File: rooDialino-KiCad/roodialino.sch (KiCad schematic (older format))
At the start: 50 parts, among them J1 Raspi Connector, J2 ICSP, J3 FTDI, J4 2nd IRX, J5 IR LED, Q1 2N7002, Q2 2N7002, Q3 2N7002, SW1 SW_Push, U1 ATmega328P, U2 TSOP34838, U3 TXS0108EPW, Y1 16 MHz

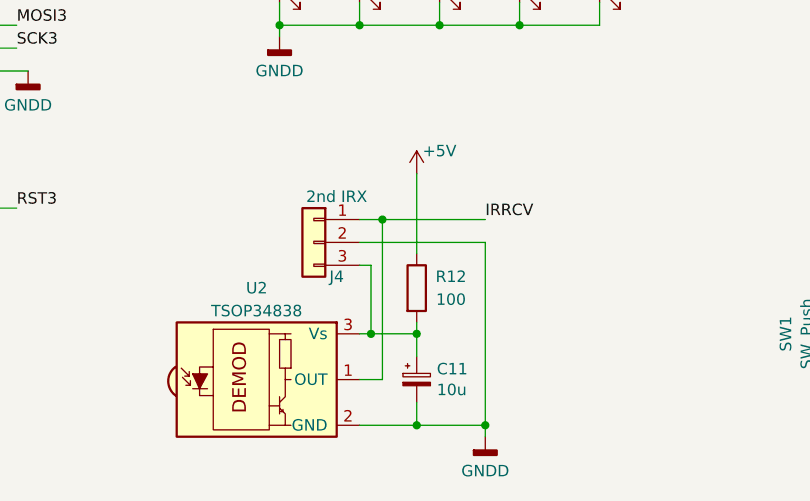
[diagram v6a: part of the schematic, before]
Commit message: Reroute to 0402 complete. Also, bugs fixed
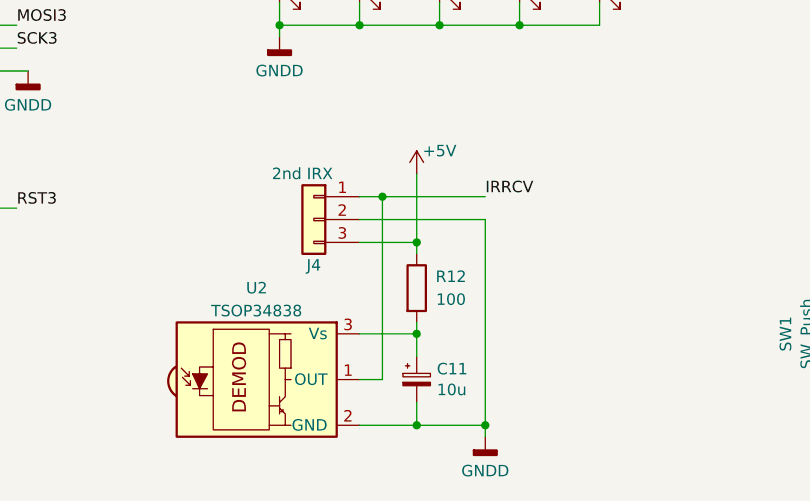
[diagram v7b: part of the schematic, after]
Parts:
- C10, C12, C3, C6, C9: footprint Capacitor_SMD:C_0603_1608Metric -> Capacitor_SMD:C_0402_1005Metric; LCSC C14663 -> C1525
- D4: footprint LED_SMD:LED_0805_2012Metric -> LED_SMD:LED_0603_1608Metric; LCSC C84256 -> C72038
- D5: footprint LED_SMD:LED_0805_2012Metric -> LED_SMD:LED_0603_1608Metric; LCSC C2297 -> C72043
- D6, D7, D8: LCSC (none) -> C55528
- R11: footprint Resistor_SMD:R_0805_2012Metric -> Resistor_SMD:R_0603_1608Metric; LCSC C17634 -> C25105
- R12: footprint Resistor_SMD:R_0603_1608Metric -> Resistor_SMD:R_0402_1005Metric; LCSC C2275 -> C25076
- R2, R3, R4, R5, R6: footprint Resistor_SMD:R_0805_2012Metric -> Resistor_SMD:R_0402_1005Metric; LCSC C17710 -> C25117
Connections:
- net +5V: now also J4.3 (Pin_3)
- net at C11.1, R12.2, U2.3 (Vs): no longer J4.3 (Pin_3)
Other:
- moved on the sheet: J4
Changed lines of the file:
@@
 F 0 "C6" V 3200 1500 50  0000 R CNN
 F 1 "100n" V 3300 1550 50  0000 R CNN
-F 2 "Capacitor_SMD:C_0603_1608Metric" H 3150 1350 50  0001 C CNN
+F 2 "Capacitor_SMD:C_0402_1005Metric" H 3150 1350 50  0001 C CNN
 F 3 "~" H 3150 1350 50  0001 C CNN
-F 4 "C14663" V 3150 1350 50  0001 C CNN "LCSC"
+F 4 "C1525" V 3150 1350 50  0001 C CNN "LCSC"
 	1    3150 1350
 	0    1    1    0
@@
 F 0 "D4" V 4150 5200 50  0000 R CNN
 F 1 "LED" V 4050 5200 50  0000 R CNN
-F 2 "LED_SMD:LED_0805_2012Metric" H 4100 5300 50  0001 C CNN
-F 3 "~" H 4100 5300 50  0001 C CNN
-F 4 "C84256" V 4100 5300 50  0001 C CNN "LCSC"
+F 2 "LED_SMD:LED_0603_1608Metric" H 4100 5300 50  0001 C CNN
+F 3 "https://datasheet.lcsc.com/lcsc/1810101813_Everlight-Elec-19-213-Y2C-CQ2R2L-3T-CY_C72038.pdf" H 4100 5300 50  0001 C CNN
+F 4 "C72038" V 4100 5300 50  0001 C CNN "LCSC"
 	1    4100 5300
 	0    -1   -1   0
@@
 F 0 "D5" V 4500 5200 50  0000 R CNN
 F 1 "LED" V 4400 5200 50  0000 R CNN
-F 2 "LED_SMD:LED_0805_2012Metric" H 4450 5300 50  0001 C CNN
-F 3 "~" H 4450 5300 50  0001 C CNN
-F 4 "C2297" V 4450 5300 50  0001 C CNN "LCSC"
+F 2 "LED_SMD:LED_0603_1608Metric" H 4450 5300 50  0001 C CNN
+F 3 "https://datasheet.lcsc.com/lcsc/1811101510_Everlight-Elec-19-217-GHC-YR1S2-3T_C72043.pdf" H 4450 5300 50  0001 C CNN
+F 4 "C72043" V 4450 5300 50  0001 C CNN "LCSC"
 	1    4450 5300
 	0    -1   -1   0
@@
 F 0 "R2" H 2900 4850 50  0000 C CNN
 F 1 "470" H 2900 4950 50  0000 C CNN
-F 2 "Resistor_SMD:R_0805_2012Metric" V 2980 4900 50  0001 C CNN
+F 2 "Resistor_SMD:R_0402_1005Metric" V 2980 4900 50  0001 C CNN
 F 3 "~" H 3050 4900 50  0001 C CNN
-F 4 "C17710" H 3050 4900 50  0001 C CNN "LCSC"
+F 4 "C25117" H 3050 4900 50  0001 C CNN "LCSC"
 	1    3050 4900
 	-1   0    0    1
@@
 F 0 "R3" H 3250 4850 50  0000 C CNN
 F 1 "470" H 3250 4950 50  0000 C CNN
-F 2 "Resistor_SMD:R_0805_2012Metric" V 3330 4900 50  0001 C CNN
+F 2 "Resistor_SMD:R_0402_1005Metric" V 3330 4900 50  0001 C CNN
 F 3 "~" H 3400 4900 50  0001 C CNN
-F 4 "C17710" H 3400 4900 50  0001 C CNN "LCSC"
+F 4 "C25117" H 3400 4900 50  0001 C CNN "LCSC"
 	1    3400 4900
 	-1   0    0    1
@@
 F 0 "R4" H 3600 4850 50  0000 C CNN
 F 1 "470" H 3600 4950 50  0000 C CNN
-F 2 "Resistor_SMD:R_0805_2012Metric" V 3680 4900 50  0001 C CNN
+F 2 "Resistor_SMD:R_0402_1005Metric" V 3680 4900 50  0001 C CNN
 F 3 "~" H 3750 4900 50  0001 C CNN
-F 4 "C17710" H 3750 4900 50  0001 C CNN "LCSC"
+F 4 "C25117" H 3750 4900 50  0001 C CNN "LCSC"
 	1    3750 4900
 	-1   0    0    1
@@
 F 0 "R5" H 3950 4850 50  0000 C CNN
 F 1 "470" H 3950 4950 50  0000 C CNN
-F 2 "Resistor_SMD:R_0805_2012Metric" V 4030 4900 50  0001 C CNN
+F 2 "Resistor_SMD:R_0402_1005Metric" V 4030 4900 50  0001 C CNN
 F 3 "~" H 4100 4900 50  0001 C CNN
-F 4 "C17710" H 4100 4900 50  0001 C CNN "LCSC"
+F 4 "C25117" H 4100 4900 50  0001 C CNN "LCSC"
 	1    4100 4900
 	-1   0    0    1
@@
 F 0 "R6" H 4300 4850 50  0000 C CNN
 F 1 "470" H 4300 4950 50  0000 C CNN
-F 2 "Resistor_SMD:R_0805_2012Metric" V 4380 4900 50  0001 C CNN
+F 2 "Resistor_SMD:R_0402_1005Metric" V 4380 4900 50  0001 C CNN
 F 3 "~" H 4450 4900 50  0001 C CNN
-F 4 "C17710" H 4450 4900 50  0001 C CNN "LCSC"
+F 4 "C25117" H 4450 4900 50  0001 C CNN "LCSC"
 	1    4450 4900
 	-1   0    0    1
@@
 F 1 "LED" H 4900 1900 50  0000 R CNN
 F 2 "LED_THT:LED_D5.0mm_IRBlack" H 4850 1700 50  0001 C CNN
-F 3 "~" H 4850 1700 50  0001 C CNN
+F 3 "https://datasheet.lcsc.com/lcsc/1809200025_Vishay-Intertech-TSAL6200_C55528.pdf" H 4850 1700 50  0001 C CNN
+F 4 "C55528" H 4850 1700 50  0001 C CNN "LCSC"
 	1    4850 1700
 	-1   0    0    1
@@
 F 1 "LED" H 5250 1900 50  0000 R CNN
 F 2 "LED_THT:LED_D5.0mm_Horizontal_O1.27mm_Z3.0mm_IRBlack" H 5200 1700 50  0001 C CNN
-F 3 "~" H 5200 1700 50  0001 C CNN
+F 3 "https://datasheet.lcsc.com/lcsc/1809200025_Vishay-Intertech-TSAL6200_C55528.pdf" H 5200 1700 50  0001 C CNN
+F 4 "C55528" H 5200 1700 50  0001 C CNN "LCSC"
 	1    5200 1700
 	-1   0    0    1
@@
 F 1 "LED" H 4550 1900 50  0000 R CNN
 F 2 "LED_THT:LED_D5.0mm_Horizontal_O1.27mm_Z3.0mm_IRBlack" H 4500 1700 50  0001 C CNN
-F 3 "~" H 4500 1700 50  0001 C CNN
+F 3 "https://datasheet.lcsc.com/lcsc/1809200025_Vishay-Intertech-TSAL6200_C55528.pdf" H 4500 1700 50  0001 C CNN
+F 4 "C55528" H 4500 1700 50  0001 C CNN "LCSC"
 	1    4500 1700
 	-1   0    0    1
@@
 F 0 "R11" H 5500 1350 50  0000 C CNN
 F 1 "33" H 5500 1250 50  0000 C CNN
-F 2 "Resistor_SMD:R_0805_2012Metric" V 5330 1300 50  0001 C CNN
+F 2 "Resistor_SMD:R_0603_1608Metric" V 5330 1300 50  0001 C CNN
 F 3 "~" H 5400 1300 50  0001 C CNN
-F 4 "C17634" H 5400 1300 50  0001 C CNN "LCSC"
+F 4 "C25105" H 5400 1300 50  0001 C CNN "LCSC"
 	1    5400 1300
 	1    0    0    -1
@@
 	1    0    0    -1
 $EndComp
-Text Label 3950 6400 0    50   ~ 0
+Text Label 3950 6300 0    50   ~ 0
 IRRCV
-$Comp
-L Connector_Generic:Conn_01x03 J4
-U 1 1 61933FD4
-P 3200 6500
-F 0 "J4" H 3100 6350 50  0000 C CNN
-F 1 "2nd IRX" H 3100 6700 50  0000 C CNN
-F 2 "Connector_PinHeader_2.54mm:PinHeader_1x03_P2.54mm_Vertical" H 3200 6500 50  0001 C CNN
-F 3 "~" H 3200 6500 50  0001 C CNN
-	1    3200 6500
-	-1   0    0    -1
-$EndComp
 $Comp
 L Connector_Generic:Conn_02x20_Odd_Even J1
@@
 F 0 "C3" H 2400 5150 50  0000 R CNN
 F 1 "100n" H 2600 4850 50  0000 R CNN
-F 2 "Capacitor_SMD:C_0603_1608Metric" H 2350 4950 50  0001 C CNN
+F 2 "Capacitor_SMD:C_0402_1005Metric" H 2350 4950 50  0001 C CNN
 F 3 "~" H 2350 4950 50  0001 C CNN
-F 4 "C14663" H 2350 4950 50  0001 C CNN "LCSC"
+F 4 "C1525" H 2350 4950 50  0001 C CNN "LCSC"
 	1    2350 4950
 	1    0    0    -1
@@
 F 0 "C9" H 5250 1100 50  0000 R CNN
 F 1 "100n" H 5300 950 50  0000 R CNN
-F 2 "Capacitor_SMD:C_0603_1608Metric" H 5050 1050 50  0001 C CNN
+F 2 "Capacitor_SMD:C_0402_1005Metric" H 5050 1050 50  0001 C CNN
 F 3 "~" H 5050 1050 50  0001 C CNN
-F 4 "C14663" H 5050 1050 50  0001 C CNN "LCSC"
+F 4 "C1525" H 5050 1050 50  0001 C CNN "LCSC"
 	1    5050 1050
 	1    0    0    -1
@@
 F 0 "C12" H 6500 4300 50  0000 R CNN
 F 1 "100n" H 6550 4200 50  0000 R CNN
-F 2 "Capacitor_SMD:C_0603_1608Metric" H 6300 4250 50  0001 C CNN
+F 2 "Capacitor_SMD:C_0402_1005Metric" H 6300 4250 50  0001 C CNN
 F 3 "~" H 6300 4250 50  0001 C CNN
-F 4 "C14663" H 6300 4250 50  0001 C CNN "LCSC"
+F 4 "C1525" H 6300 4250 50  0001 C CNN "LCSC"
 	1    6300 4250
 	1    0    0    -1
@@
 F 0 "C10" H 5800 4300 50  0000 R CNN
 F 1 "100n" H 5850 4200 50  0000 R CNN
-F 2 "Capacitor_SMD:C_0603_1608Metric" H 5900 4250 50  0001 C CNN
+F 2 "Capacitor_SMD:C_0402_1005Metric" H 5900 4250 50  0001 C CNN
 F 3 "~" H 5900 4250 50  0001 C CNN
-F 4 "C14663" H 5900 4250 50  0001 C CNN "LCSC"
+F 4 "C1525" H 5900 4250 50  0001 C CNN "LCSC"
 	1    5900 4250
 	1    0    0    -1
@@
 F 0 "R12" H 3800 6750 50  0000 C CNN
 F 1 "100" H 3800 6650 50  0000 C CNN
-F 2 "Resistor_SMD:R_0603_1608Metric" V 3580 6700 50  0001 C CNN
+F 2 "Resistor_SMD:R_0402_1005Metric" V 3580 6700 50  0001 C CNN
 F 3 "~" H 3650 6700 50  0001 C CNN
-F 4 "C2275" H 3650 6700 50  0001 C CNN "LCSC"
+F 4 "C25076" H 3650 6700 50  0001 C CNN "LCSC"
 	1    3650 6700
 	1    0    0    -1
@@
 $EndComp
 Wire Wire Line
-	3400 6900 3450 6900
-Wire Wire Line
-	3450 6900 3450 6600
-Wire Wire Line
-	3450 6600 3400 6600
-Wire Wire Line
 	3400 7300 3650 7300
-Wire Wire Line
-	3950 7300 3950 6500
-Wire Wire Line
-	3950 6500 3400 6500
 Wire Wire Line
 	3950 7300 3950 7350
@@
 Wire Wire Line
 	3400 7100 3500 7100
-Wire Wire Line
-	3500 6400 3400 6400
 $Comp
 L Device:CP_Small C11
@@
 $EndComp
 Wire Wire Line
-	3500 6400 3500 7100
+	3500 6300 3500 7100
 Wire Wire Line
 	3650 7200 3650 7300
@@
 	3650 7000 3650 6900
 Wire Wire Line
-	3650 6900 3450 6900
-Connection ~ 3450 6900
-Wire Wire Line
 	3650 6900 3650 6850
 Connection ~ 3650 6900
 Wire Wire Line
-	3500 6400 3950 6400
-Connection ~ 3500 6400
-Wire Wire Line
-	3650 6200 3650 6550
+	3500 6300 3950 6300
+Wire Wire Line
+	3650 6200 3650 6500
+Wire Wire Line
+	3400 6900 3650 6900
+$Comp
+L Connector_Generic:Conn_01x03 J4
+U 1 1 61933FD4
+P 3200 6400
+F 0 "J4" H 3200 6200 50  0000 C CNN
+F 1 "2nd IRX" H 3250 6600 50  0000 C CNN
+F 2 "Connector_PinHeader_2.54mm:PinHeader_1x03_P2.54mm_Vertical" H 3200 6400 50  0001 C CNN
+F 3 "~" H 3200 6400 50  0001 C CNN
+	1    3200 6400
+	-1   0    0    -1
+$EndComp
+Wire Wire Line
+	3400 6300 3500 6300
+Connection ~ 3500 6300
+Wire Wire Line
+	3400 6400 3950 6400
+Wire Wire Line
+	3950 6400 3950 7300
+Wire Wire Line
+	3400 6500 3650 6500
+Connection ~ 3650 6500
+Wire Wire Line
+	3650 6500 3650 6550
 $EndSCHEMATC

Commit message: Some final (?) bling
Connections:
- net at D8.1 (K), Q1.3 (D): now also J5.1 (Pin_1); no longer J5.2 (Pin_2)
- net at R11.2: now also J5.2 (Pin_2); no longer J5.1 (Pin_1)
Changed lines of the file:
@@
-	1    0    0    -1
-$EndComp
-$Comp
-L Connector_Generic:Conn_01x02 J5
-U 1 1 61A1AF2A
-P 5600 1600
-F 0 "J5" H 5680 1592 50  0000 L CNN
-F 1 "IR LED" H 5680 1501 50  0000 L CNN
-F 2 "Connector_PinHeader_2.54mm:PinHeader_1x02_P2.54mm_Vertical" H 5600 1600 50  0001 C CNN
-F 3 "~" H 5600 1600 50  0001 C CNN
-	1    5600 1600
 	1    0    0    -1
 $EndComp
@@
 Wire Wire Line
 	5400 1700 5400 1900
-Connection ~ 5400 1700
-Wire Wire Line
-	5400 1600 5400 1450
 Wire Wire Line
 	4300 1450 4300 1700
@@
 Wire Wire Line
 	3650 6500 3650 6550
+Connection ~ 5400 1700
+Wire Wire Line
+	5400 1600 5400 1450
+$Comp
+L Connector_Generic:Conn_01x02 J5
+U 1 1 61A1AF2A
+P 5600 1700
+F 0 "J5" H 5680 1692 50  0000 L CNN
+F 1 "IR LED" H 5680 1601 50  0000 L CNN
+F 2 "Connector_PinHeader_2.54mm:PinHeader_1x02_P2.54mm_Vertical" H 5600 1700 50  0001 C CNN
+F 3 "~" H 5600 1700 50  0001 C CNN
+	1    5600 1700
+	1    0    0    1
+$EndComp
 $EndSCHEMATC
